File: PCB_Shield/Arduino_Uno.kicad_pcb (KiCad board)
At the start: 2 copper layers, 68.6 x 53.3 mm, 8 parts, among them J1 Power, J2 Digital/PWM, J3 Analog, J4 Digital/PWM

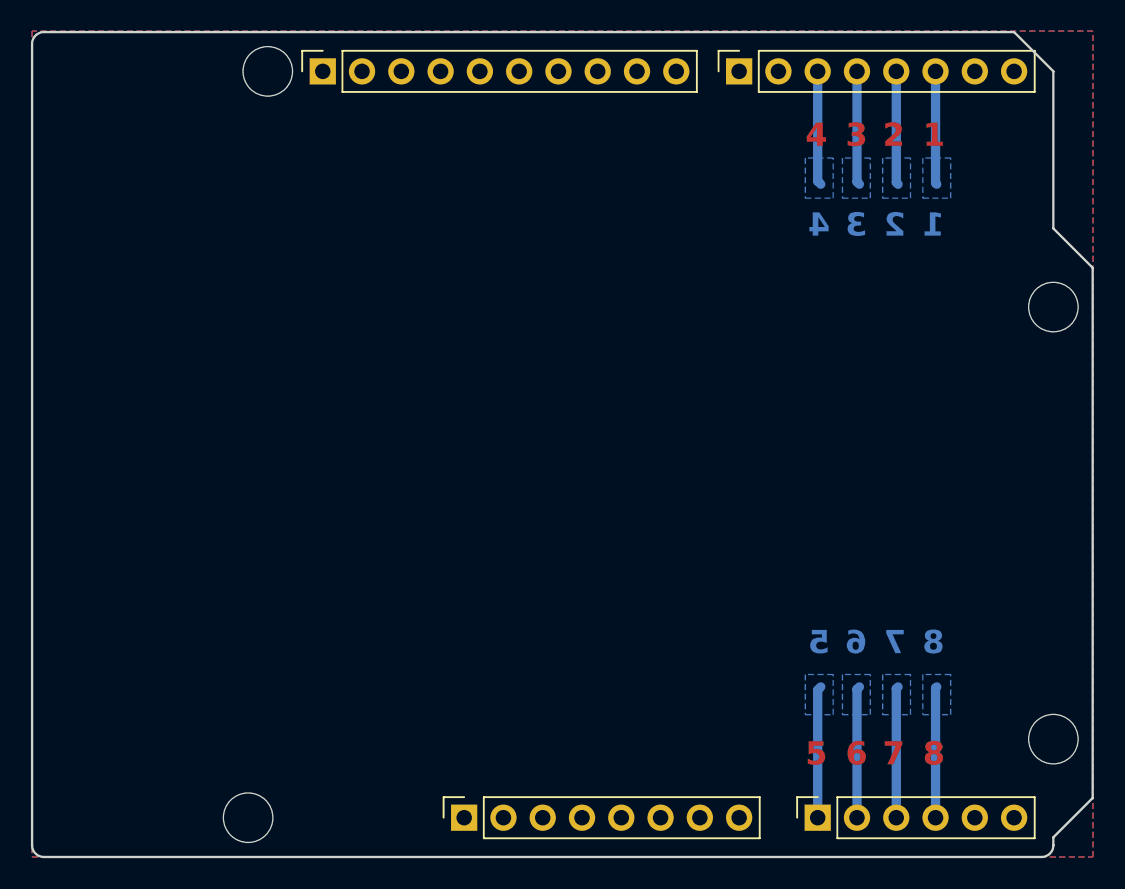
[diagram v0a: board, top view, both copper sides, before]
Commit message: holes insted of pads for soldering
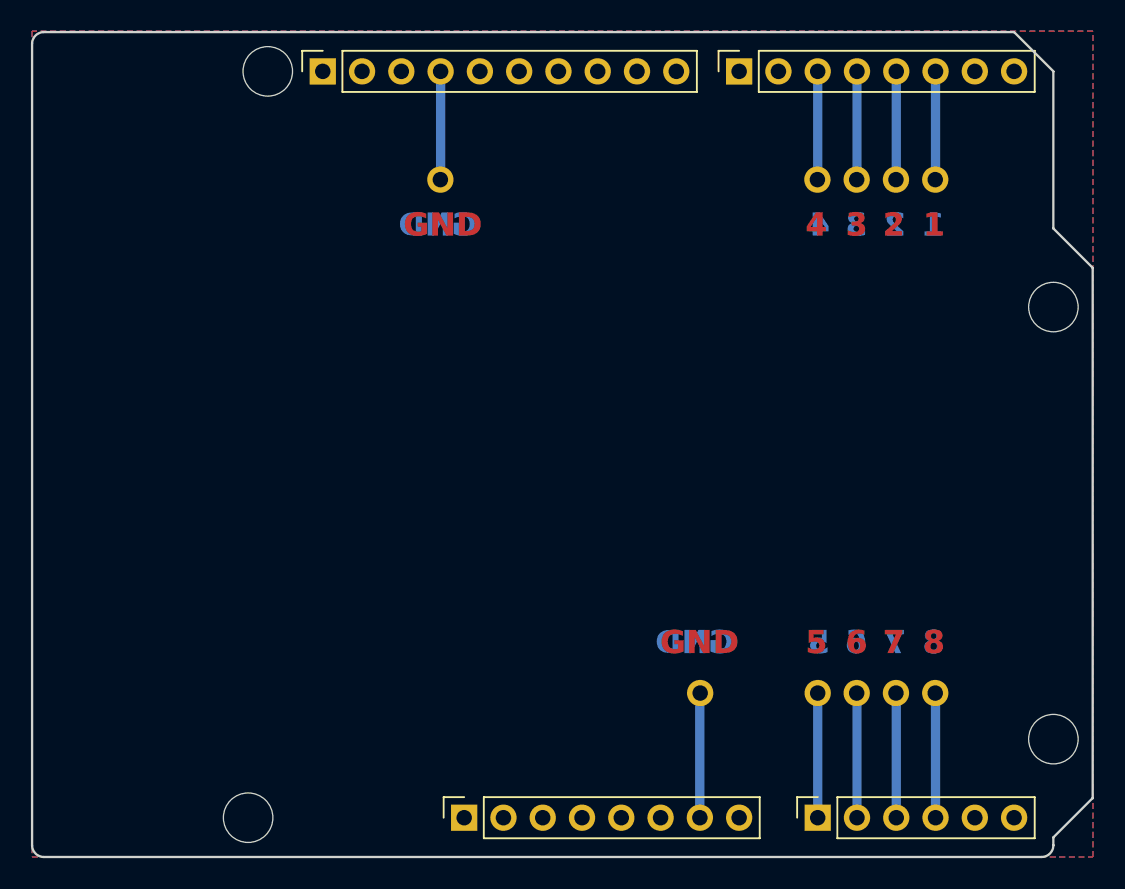
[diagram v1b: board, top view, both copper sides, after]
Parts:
- added ?: , , F.Cu at (150.8, 56.2)
- added ?: , , F.Cu at (158.4, 89.4)
- added ?: , , F.Cu at (126.4, 56.2)
- added ?: , , F.Cu at (153.3, 56.2)
- added ?: , , F.Cu at (155.9, 89.4)
- added ?: , , F.Cu at (143.2, 89.4)
- added ?: , , F.Cu at (158.4, 56.2)
- added ?: , , F.Cu at (155.9, 56.2)
- added ?: , , F.Cu at (153.3, 89.4)
- added ?: , , F.Cu at (150.8, 89.4)
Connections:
- net /SCL/A5 renamed /A5
- net /SDA/A4 renamed /A4
- J2 pad 1: (no net) -> /SCL
- J2 pad 2: (no net) -> /SDA
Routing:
- net GND: track 0.00 -> 15.1 mm
- removed copper zone on B.Cu, net /*3
- removed copper zone on B.Cu, net /*5
- removed copper zone on B.Cu, net /2
- removed copper zone on B.Cu, net /4
- removed copper zone on B.Cu, net /A0
- removed copper zone on B.Cu, net /A1
- removed copper zone on B.Cu, net /A2
- removed copper zone on B.Cu, net /A3
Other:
- board text added: "GND"
